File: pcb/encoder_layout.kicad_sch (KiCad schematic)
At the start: 10 parts

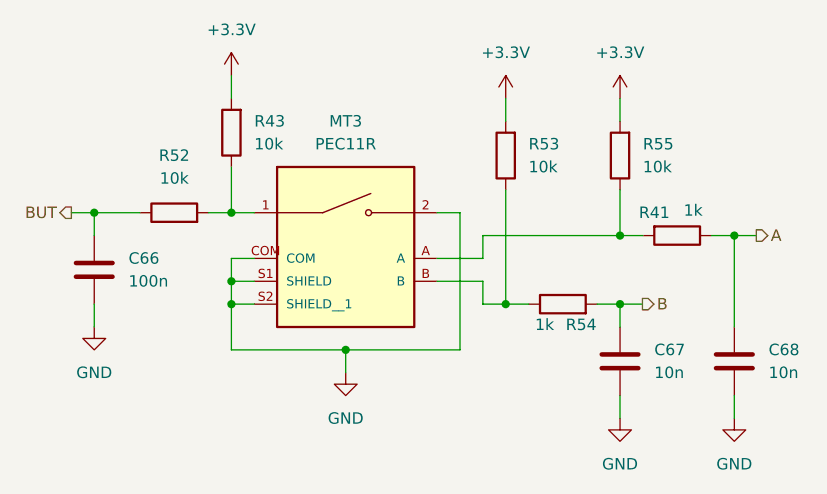
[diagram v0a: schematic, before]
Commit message: rework to tia feedback selection, board power, and ui
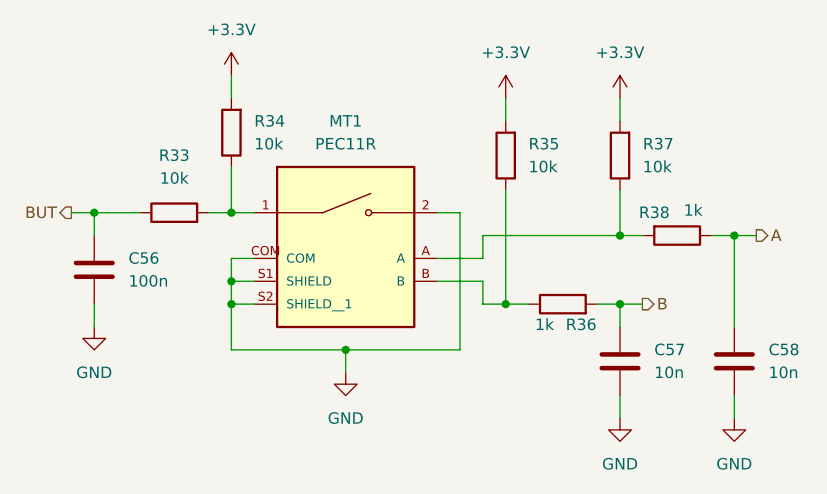
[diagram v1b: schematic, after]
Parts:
- renumbered C66 to C56, C67 to C57, C68 to C58, MT3 to MT1, R52 to R33, R43 to R34, R53 to R35, R54 to R36, R55 to R37, R41 to R38
